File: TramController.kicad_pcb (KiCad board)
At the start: 2 copper layers, 76.5 x 54.5 mm, 35 parts, among them J1 Screw_Terminal_01x04, J2 power, J3 Screw_Terminal_01x04, J4 servo, J5 servo, J6 power, K1 SANYOU_SRD_Form_C, Q1 BC547, U1 EL814, U2 L298HN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

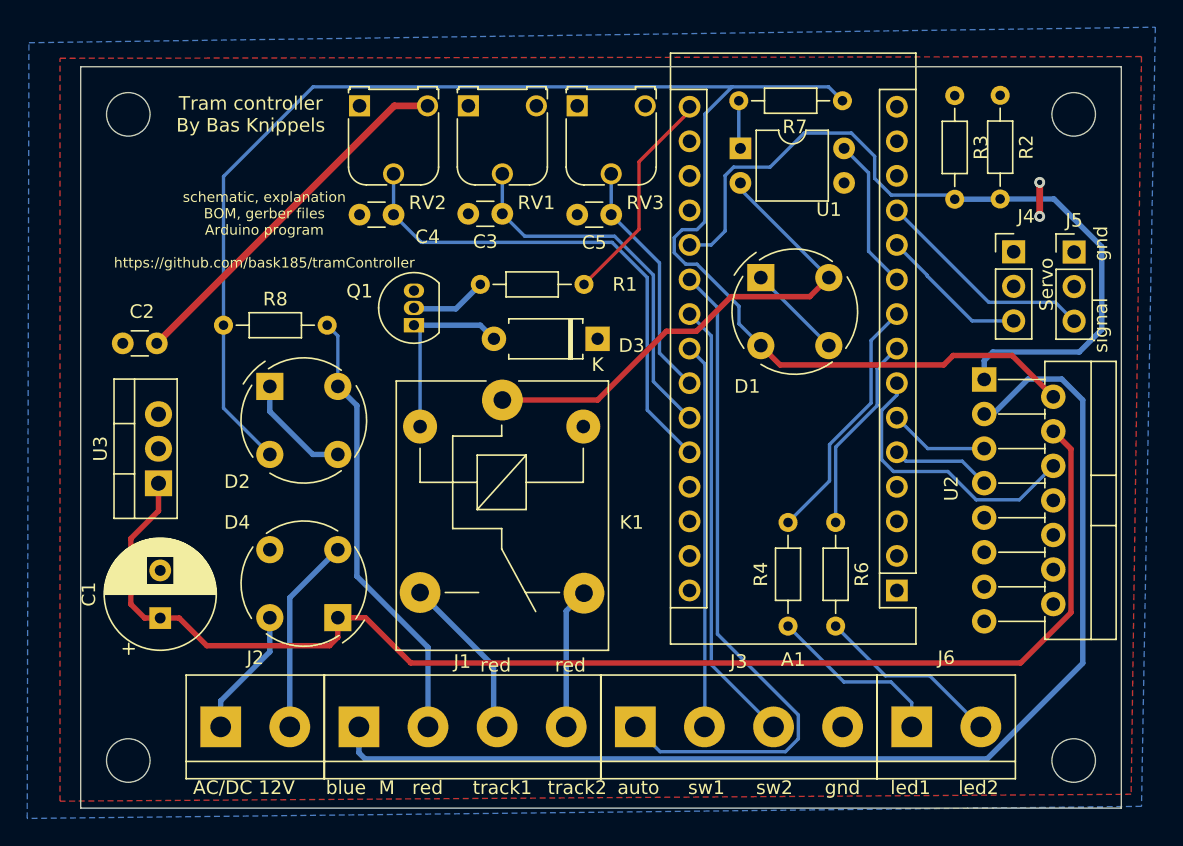
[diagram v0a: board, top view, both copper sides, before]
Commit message: replaced schematic with a more up to date one
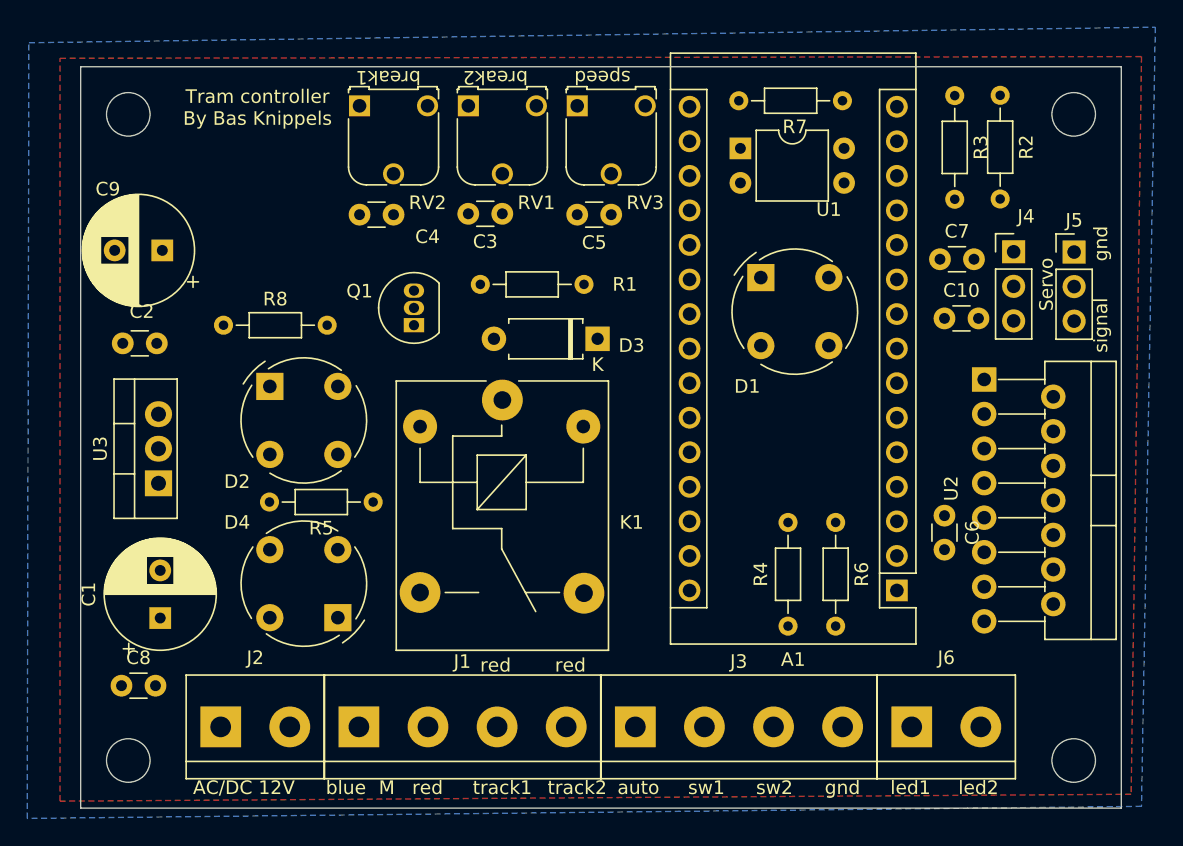
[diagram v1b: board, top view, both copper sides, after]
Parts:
- added C10: 100nF, Capacitor_THT:C_Disc_D3.0mm_W1.6mm_P2.50mm, F.Cu at (111.5, 67.0)
- added C6: 100nF, Capacitor_THT:C_Disc_D3.0mm_W1.6mm_P2.50mm, F.Cu at (111.5, 81.5)
- added C7: 100nF, Capacitor_THT:C_Disc_D3.0mm_W1.6mm_P2.50mm, F.Cu at (111.2, 62.6)
- added C8: 100nF, Capacitor_THT:C_Disc_D3.0mm_W1.6mm_P2.50mm, F.Cu at (51.0, 94.0)
- added C9: 1000uF, Capacitor_THT:CP_Radial_D8.0mm_P3.50mm, F.Cu at (54.0, 62.0)
- added R5: 4k7, Resistor_THT:R_Axial_DIN0204_L3.6mm_D1.6mm_P7.62mm_Horizontal, F.Cu at (69.5, 80.5)
- C1: value CP -> 1000uF
- C2: value C -> 100nF
- J1: value Screw_Terminal_01x04 -> to Tracks
- J3: value Screw_Terminal_01x04 -> control panel
- K1: value SANYOU_SRD_Form_C -> SPST
- R1: value R -> 1k
- R2, R3: value R -> 1R
- R7: value R -> 33R
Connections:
- net /currentSense renamed /shortCircuit
- net /front renamed /frontTrack
- net /rear renamed /rearTrack
- net /red renamed /redIn
- net Net-(A1-Pad13) renamed /JP1
- net Net-(A1-Pad14) renamed /JP2
- net Net-(A1-Pad15) renamed /JP3
- net Net-(A1-Pad16) renamed /relayPin
- net Net-(D1-Pad4) renamed /slidings
- net Net-(D2-Pad4) renamed /redOut
- A1 pad 22: /sw2 -> /sw1
- A1 pad 23: /sw1 -> /sw2
- U2 pad 10: Net-(U2-Pad10) -> GND
- U2 pad 11: Net-(U2-Pad11) -> GND
- U2 pad 12: Net-(U2-Pad12) -> GND
- U2 pad 15: Net-(U2-Pad15) -> GND
- U2 pad 4: VCC -> +5V
- U2 pad 9: GND -> VCC
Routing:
- net /redIn: track 118.7 -> 0.00 mm
- net VCC: track 98.6 -> 0.00 mm
- net /blue: track 86.5 -> 0.00 mm
- net /shortCircuit: track 57.6 -> 0.00 mm
- net /auto_manual: track 50.2 -> 0.00 mm
- net /runout2: track 37.7 -> 0.00 mm
- net /slidings: track 37.4 -> 0.00 mm
- net /sw2: track 32.9 -> 0.00 mm
- net /redOut: track 32.6 -> 0.00 mm
- net +5V: track 29.6 -> 0.00 mm, vias 2 -> 0
- net /sw1: track 28.3 -> 0.00 mm
- net /runout1: track 27.5 -> 0.00 mm
- net /enable: track 21.0 -> 0.00 mm
- net /status1: track 18.6 -> 0.00 mm
- net /speed: track 17.8 -> 0.00 mm
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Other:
- board text added: "break1"
- board text added: "break2"
- board text added: "speed"
